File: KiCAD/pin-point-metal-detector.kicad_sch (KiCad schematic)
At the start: 10 parts, among them Q1 2N3904

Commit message: first version
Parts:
- removed C2: 1nF, symbol Device:C
- removed C5: 2n2, symbol Device:C
- removed Q1: 2N3904, Package_TO_SOT_THT:TO-92_Inline, symbol Transistor_BJT:2N3904
- added BT1: 4xAA, symbol Device:Battery
- added C2: 47uF, symbol Device:C_Polarized
- added D1: 1N4001, Diode_THT:D_DO-41_SOD81_P10.16mm_Horizontal, symbol Diode:1N4001
- added D2: GREEN LED, symbol Device:LED
- added D3: 1N4148, Diode_THT:D_DO-35_SOD27_P7.62mm_Horizontal, symbol Diode:1N4148
- added LS1: 130 OHM, symbol Device:Speaker
- added SW1: Power, symbol Switch:SW_SPST
- C1: value 1uF -> 100nF
- C3: value 2n2 -> 1uF
- C4: value 2n2 -> 1nF
- L1: value 64uH -> 10mH
- R1: value 15K -> 76
- R2: value 5K6 -> 10K
- R3: value 120 -> 330
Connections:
- net +6Volt: now also D1.2 (A), SW1.2 (B); no longer C3.2, L1.1, R1.1
- net GND: now also C1.1, C3.2, L1.2, BT1.2 (-), D2.1 (K), LS1.2; no longer C1.2, R3.2
- net T1CH4: now reaches R3.1
- net at C4.2: now also L1.1; no longer L1.2
- net at C4.1: now also R3.2, D3.2 (A); no longer C3.1
- new net: D2.2 (A), R1.1
- new net: C2.2, LS1.1
- new net: BT1.1 (+), SW1.1 (A)
- new net 5.4v: D1.1 (K)
- new net D3: C1.2, C3.1, D3.1 (K), R2.1
- new net D4: C2.1
- new net D7: R1.2
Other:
- note added: "Fr (résonance)=50329 Hertz"
- note added: "NUCLEO-8S207K8"
- note added: "https://creativecommons.org/licenses/by-sa/4.0/legalcode"
- note added: "pin point metal detector Jacques Deschênes, 2023 licence: CC BY-SA"

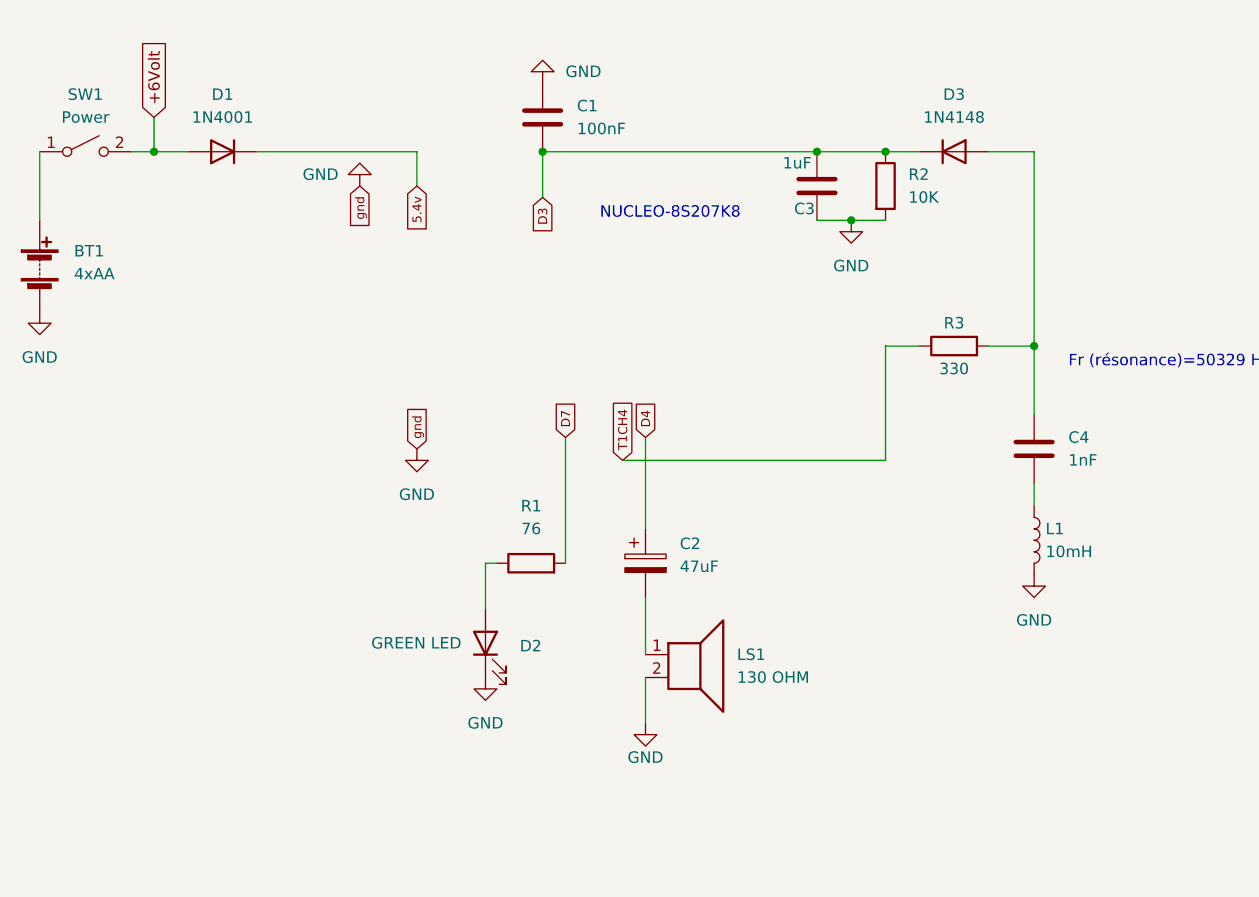
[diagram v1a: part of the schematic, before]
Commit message: Ajout du journal et mise à jour du readme.md
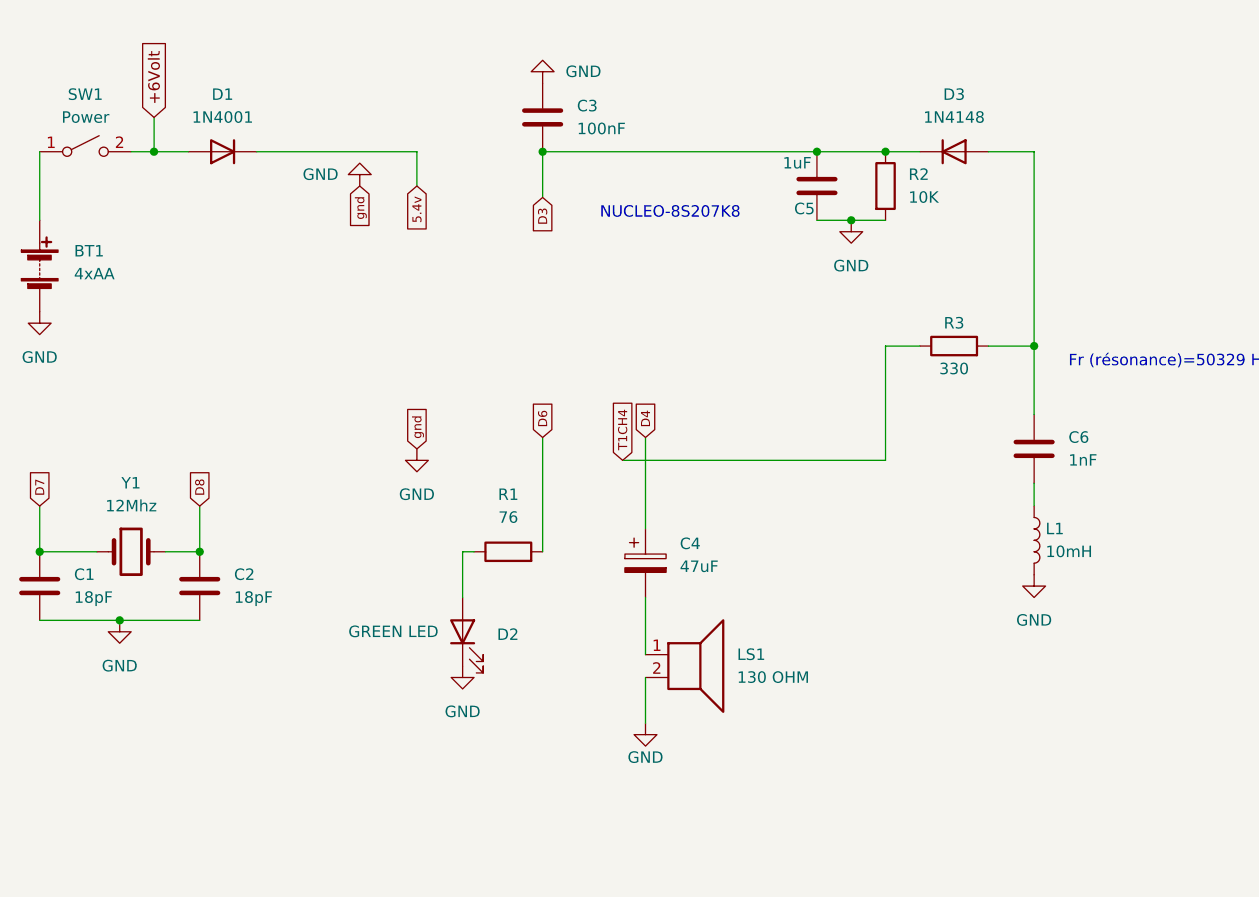
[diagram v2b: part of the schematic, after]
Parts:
- added C1, C2: 18pF, symbol Device:C
- added Y1: 12Mhz, symbol Device:Crystal
- renumbered C1 to C3, C2 to C4, C3 to C5, C4 to C6
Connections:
- net D7: now also C1.1, Y1.1; no longer R1.2
- net GND: now also C1.2, C2.2
- new net D6: R1.2
- new net D8: C2.1, Y1.2
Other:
- moved on the sheet: D2, R1

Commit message: version 1 révison 2
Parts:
- removed C5: 1uF, symbol Device:C
- added C2: 10uF, symbol Device:C_Polarized
- C5: renamed from C4; value 47uF -> 10uF
- R2: value 10K -> 5M1
- renumbered C2 to C3, C3 to C4
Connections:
- net +6Volt: now also C2.1
- net GND: now also C2.2
- net D3 renamed A3
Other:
- note added: "metal-pointer Rev. 2"
- moved on the sheet: BT1, C1, C3, C4, C5, C6, D1, D2, D3, L1, LS1, R1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

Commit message: Modification au circuit
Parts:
- added J1: batt. con., symbol Connector:Conn_01x02_Female
- added J2: circuit con., symbol Connector:Conn_01x02_Male
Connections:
- net +6Volt: now also J2.1 (Pin_1); no longer SW1.2 (B)
- net GND: now also J2.2 (Pin_2); no longer BT1.2 (-)
- net 5.4v renamed 5.3v
- new net: J1.1 (Pin_1), SW1.2 (B)
- new net: BT1.2 (-), J1.2 (Pin_2)
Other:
- note added: "metal-pointer Rev. 3"
- note removed: "metal-pointer Rev. 2"
- moved on the sheet: BT1, SW1
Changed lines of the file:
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@@
   (junction (at 111.76 101.6) (diameter 0) (color 0 0 0 0)
   )
-  (junction (at 154.94 101.6) (diameter 0) (color 0 0 0 0)
-  )
   (junction (at 104.14 101.6) (diameter 0) (color 0 0 0 0)
   )
+  (junction (at 154.94 101.6) (diameter 0) (color 0 0 0 0)
+  )
   (junction (at 99.06 146.05) (diameter 0) (color 0 0 0 0)
   )
@@
   (junction (at 189.23 101.6) (diameter 0) (color 0 0 0 0)
   )
+  (wire (pts (xy 96.52 104.14) (xy 96.52 113.03))
+    (stroke (width 0) (type default) (color 0 0 0 0))
+  )
   (wire (pts (xy 104.14 101.6) (xy 104.14 105.41))
     (stroke (width 0) (type default) (color 0 0 0 0))
@@
     (stroke (width 0) (type default) (color 0 0 0 0))
   )
+  (wire (pts (xy 67.31 119.38) (xy 82.55 119.38))
+    (stroke (width 0) (type default) (color 0 0 0 0))
+  )
   (wire (pts (xy 99.06 140.97) (xy 99.06 146.05))
     (stroke (width 0) (type default) (color 0 0 0 0))
@@
     (stroke (width 0) (type default) (color 0 0 0 0))
   )
+  (wire (pts (xy 132.08 101.6) (xy 132.08 104.14))
+    (stroke (width 0) (type default) (color 0 0 0 0))
+  )
+  (wire (pts (xy 77.47 101.6) (xy 82.55 101.6))
+    (stroke (width 0) (type default) (color 0 0 0 0))
+  )
   (wire (pts (xy 193.04 135.89) (xy 193.04 123.19))
     (stroke (width 0) (type default) (color 0 0 0 0))
@@
     (stroke (width 0) (type default) (color 0 0 0 0))
   )
-  (wire (pts (xy 90.17 101.6) (xy 90.17 109.22))
+  (wire (pts (xy 67.31 101.6) (xy 67.31 109.22))
     (stroke (width 0) (type default) (color 0 0 0 0))
   )
@@
     (stroke (width 0) (type default) (color 0 0 0 0))
   )
-  (wire (pts (xy 100.33 101.6) (xy 104.14 101.6))
+  (wire (pts (xy 96.52 101.6) (xy 104.14 101.6))
     (stroke (width 0) (type default) (color 0 0 0 0))
   )
@@
     (stroke (width 0) (type default) (color 0 0 0 0))
   )
-  (wire (pts (xy 123.19 101.6) (xy 140.97 101.6))
+  (wire (pts (xy 154.94 101.6) (xy 154.94 106.68))
     (stroke (width 0) (type default) (color 0 0 0 0))
   )
-  (wire (pts (xy 140.97 101.6) (xy 140.97 105.41))
+  (wire (pts (xy 82.55 119.38) (xy 82.55 104.14))
     (stroke (width 0) (type default) (color 0 0 0 0))
   )
-  (wire (pts (xy 154.94 101.6) (xy 154.94 106.68))
+  (wire (pts (xy 113.03 146.05) (xy 116.84 146.05))
     (stroke (width 0) (type default) (color 0 0 0 0))
   )
-  (wire (pts (xy 113.03 146.05) (xy 116.84 146.05))
+  (wire (pts (xy 123.19 101.6) (xy 132.08 101.6))
     (stroke (width 0) (type default) (color 0 0 0 0))
   )
@@
     (effects (font (size 2 2)) (justify left bottom))
   )
-  (text "NUCLEO-8S207K8" (at 161.29 109.22 0)
+  (text "NUCLEO-8S207K8" (at 120.65 133.35 0)
     (effects (font (size 1.27 1.27)) (justify left bottom))
   )
-  (text "metal-pointer Rev. 2\n" (at 189.23 190.5 0)
+  (text "metal-pointer Rev. 3\n" (at 189.23 190.5 0)
     (effects (font (size 2 2)) (justify left bottom))
   )
@@
     )
   )
-  (global_label "5.4v" (shape input) (at 140.97 105.41 270) (fields_autoplaced)
+  (global_label "5.3v" (shape input) (at 132.08 104.14 270) (fields_autoplaced)
     (effects (font (size 1 1)) (justify right))
-    (property "Références Inter-Feuilles" "${INTERSHEET_REFS}" (id 0) (at 140.9075 110.4529 90)
+    (property "Références Inter-Feuilles" "${INTERSHEET_REFS}" (id 0) (at 132.0175 109.1829 90)
       (effects (font (size 1 1)) (justify right) hide)
     )
   )
+  (symbol (lib_id "Connector:Conn_01x02_Female") (at 87.63 101.6 0) (unit 1)
+    (in_bom yes) (on_board yes)
+    (property "Reference" "J1" (id 0) (at 85.09 106.68 0)
+      (effects (font (size 1.27 1.27)) (justify left))
+    )
+    (property "Value" "batt. con." (id 1) (at 78.74 99.06 0)
+      (effects (font (size 1.27 1.27)) (justify left))
+    )
+    (property "Footprint" "" (id 2) (at 87.63 101.6 0)
+      (effects (font (size 1.27 1.27)) hide)
+    )
+    (property "Datasheet" "~" (id 3) (at 87.63 101.6 0)
+      (effects (font (size 1.27 1.27)) hide)
+    )
+    (pin "1")
+    (pin "2")
+  )
   (symbol (lib_id "power:GND") (at 104.14 113.03 0) (unit 1)
     (in_bom yes) (on_board yes) (fields_autoplaced)
@@
     (pin "2")
   )
+  (symbol (lib_id "Connector:Conn_01x02_Male") (at 91.44 101.6 0) (unit 1)
+    (in_bom yes) (on_board yes)
+    (property "Reference" "J2" (id 0) (at 91.44 106.68 0))
+    (property "Value" "circuit con." (id 1) (at 95.25 99.06 0))
+    (property "Footprint" "" (id 2) (at 91.44 101.6 0)
+      (effects (font (size 1.27 1.27)) hide)
+    )
+    (property "Datasheet" "~" (id 3) (at 91.44 101.6 0)
+      (effects (font (size 1.27 1.27)) hide)
+    )
+    (pin "1")
+    (pin "2")
+  )
   (symbol (lib_id "Device:R") (at 151.13 146.05 90) (unit 1)
     (in_bom yes) (on_board yes) (fields_autoplaced)
@@
     (pin "2")
   )
-  (symbol (lib_id "Device:Battery") (at 90.17 114.3 0) (unit 1)
+  (symbol (lib_id "Device:Battery") (at 67.31 114.3 0) (unit 1)
     (in_bom yes) (on_board yes) (fields_autoplaced)
-    (property "Reference" "BT1" (id 0) (at 93.98 112.6489 0)
+    (property "Reference" "BT1" (id 0) (at 71.12 112.6489 0)
       (effects (font (size 1.27 1.27)) (justify left))
     )
-    (property "Value" "4xAA" (id 1) (at 93.98 115.1889 0)
+    (property "Value" "4xAA" (id 1) (at 71.12 115.1889 0)
       (effects (font (size 1.27 1.27)) (justify left))
     )
-    (property "Footprint" "" (id 2) (at 90.17 112.776 90)
+    (property "Footprint" "" (id 2) (at 67.31 112.776 90)
       (effects (font (size 1.27 1.27)) hide)
     )
-    (property "Datasheet" "~" (id 3) (at 90.17 112.776 90)
+    (property "Datasheet" "~" (id 3) (at 67.31 112.776 90)
       (effects (font (size 1.27 1.27)) hide)
     )
@@
       (effects (font (size 1.27 1.27)) hide)
     )
-    (property "Value" "GND" (id 1) (at 128.27 104.14 0)
+    (property "Value" "GND" (id 1) (at 132.08 100.33 0)
       (effects (font (size 1.27 1.27)) (justify right))
     )
@@
     (pin "2")
   )
+  (symbol (lib_id "power:GND") (at 96.52 113.03 0) (unit 1)
+    (in_bom yes) (on_board yes) (fields_autoplaced)
+    (property "Reference" "#PWR01" (id 0) (at 96.52 119.38 0)
+      (effects (font (size 1.27 1.27)) hide)
+    )
+    (property "Value" "GND" (id 1) (at 96.52 118.11 0))
+    (property "Footprint" "" (id 2) (at 96.52 113.03 0)
+      (effects (font (size 1.27 1.27)) hide)
+    )
+    (property "Datasheet" "" (id 3) (at 96.52 113.03 0)
+      (effects (font (size 1.27 1.27)) hide)
+    )
+    (pin "1")
+  )
   (symbol (lib_id "Device:LED") (at 146.05 154.94 90) (unit 1)
     (in_bom yes) (on_board yes)
@@
     (pin "2")
   )
-  (symbol (lib_id "power:GND") (at 90.17 119.38 0) (unit 1)
-    (in_bom yes) (on_board yes) (fields_autoplaced)
-    (property "Reference" "#PWR01" (id 0) (at 90.17 125.73 0)
-      (effects (font (size 1.27 1.27)) hide)
-    )
-    (property "Value" "GND" (id 1) (at 90.17 124.46 0))
-    (property "Footprint" "" (id 2) (at 90.17 119.38 0)
-      (effects (font (size 1.27 1.27)) hide)
-    )
-    (property "Datasheet" "" (id 3) (at 90.17 119.38 0)
-      (effects (font (size 1.27 1.27)) hide)
-    )
-    (pin "1")
-  )
-  (symbol (lib_id "Switch:SW_SPST") (at 95.25 101.6 0) (unit 1)
+  (symbol (lib_id "Switch:SW_SPST") (at 72.39 101.6 0) (unit 1)
     (in_bom yes) (on_board yes) (fields_autoplaced)
-    (property "Reference" "SW1" (id 0) (at 95.25 95.25 0))
-    (property "Value" "Power" (id 1) (at 95.25 97.79 0))
-    (property "Footprint" "" (id 2) (at 95.25 101.6 0)
+    (property "Reference" "SW1" (id 0) (at 72.39 95.25 0))
+    (property "Value" "Power" (id 1) (at 72.39 97.79 0))
+    (property "Footprint" "" (id 2) (at 72.39 101.6 0)
       (effects (font (size 1.27 1.27)) hide)
     )
-    (property "Datasheet" "~" (id 3) (at 95.25 101.6 0)
+    (property "Datasheet" "~" (id 3) (at 72.39 101.6 0)
       (effects (font (size 1.27 1.27)) hide)
     )
@@
   )
   (symbol_instances
-    (path "/ed233888-bfd2-4d3e-9c4f-6cadf14c9baa"
+    (path "/d6e53487-70c6-4179-8894-5f2ba6b4a896"
       (reference "#PWR01") (unit 1) (value "GND") (footprint "")
     )
@@
       (reference "D3") (unit 1) (value "1N4148") (footprint "Diode_THT:D_DO-35_SOD27_P7.62mm_Horizontal")
     )
+    (path "/024a3ede-8f38-4258-a9ad-c6240c4821d9"
+      (reference "J1") (unit 1) (value "batt. con.") (footprint "")
+    )
+    (path "/35bb32fd-46f9-4df5-bfbe-9d1f3f5b0784"
+      (reference "J2") (unit 1) (value "circuit con.") (footprint "")
+    )
     (path "/47b1c576-34d1-461a-9136-a0e33dcd8240"
